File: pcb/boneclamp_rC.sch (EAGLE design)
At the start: 129 parts, among them IC1 24C, U1 AD8032ARZ-REEL7, U10 ADA4841-2YRZ, U11 ADA4841-2YRZ, U2 LT1964ES5-5TRMPBF, U3 ADA4841-2YRZ, U4 TLV70245DBVT, U5 ADA4841-2YRZ, U6 AD713JRZ-16, U7 AD7682BCPZ, U8 TPS63700DRCT, U9 ADA4841-2YRZ

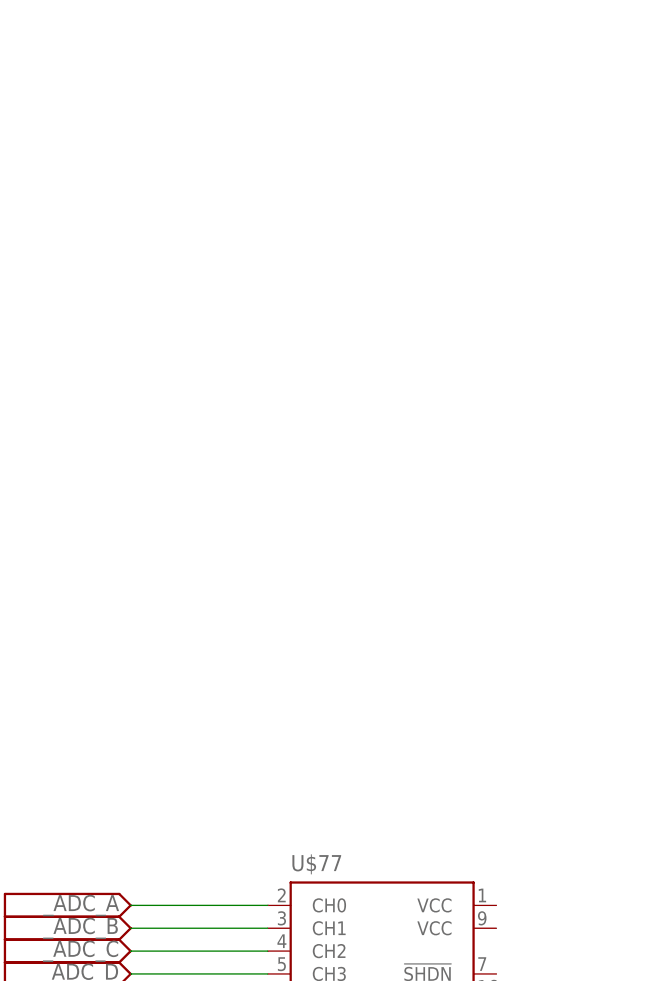
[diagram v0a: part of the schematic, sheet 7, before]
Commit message: Added the 8331 to schematic. I'm pretty sure this is the right ADC.
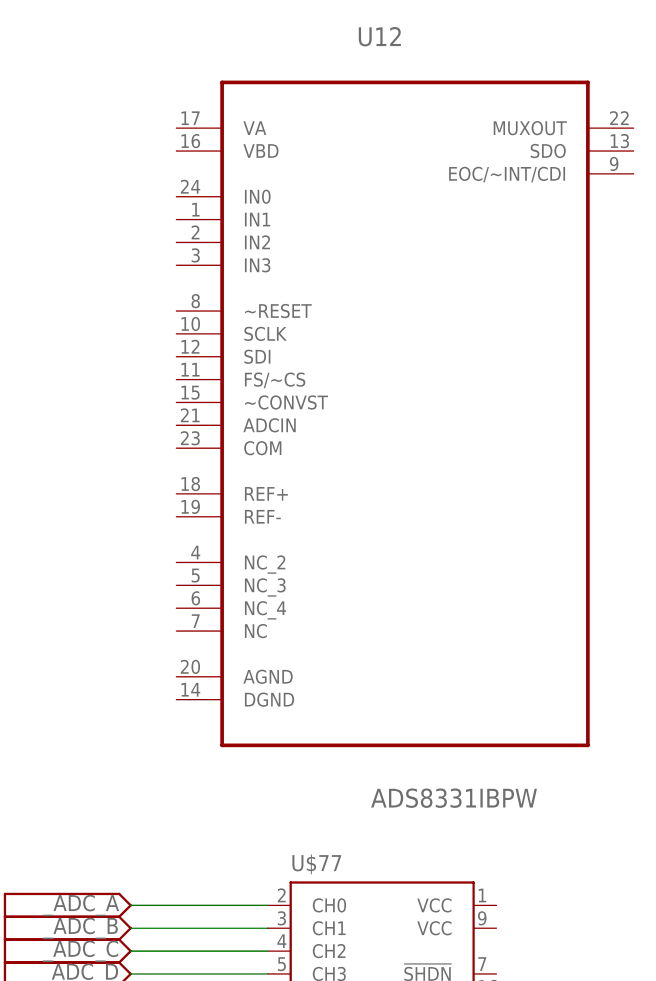
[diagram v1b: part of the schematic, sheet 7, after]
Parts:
- added U12: ADS8331IBPW, ti-extended:ADS8331IBPW
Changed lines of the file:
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@@
 <part name="U$76" library="boneclamp" deviceset="V_SIG" device=""/>
 <part name="U$82" library="boneclamp" deviceset="V_SIG" device=""/>
+<part name="U12" library="ti-extended" deviceset="ADS8331IBPW" device=""/>
 </parts>
 <sheets>
@@
 <instance part="U$80" gate="G$1" x="-27.94" y="7.62" rot="MR0"/>
 <instance part="U$81" gate="G$1" x="-27.94" y="5.08" rot="MR0"/>
+<instance part="U12" gate="A" x="2.54" y="71.12"/>
 </instances>
 <busses>

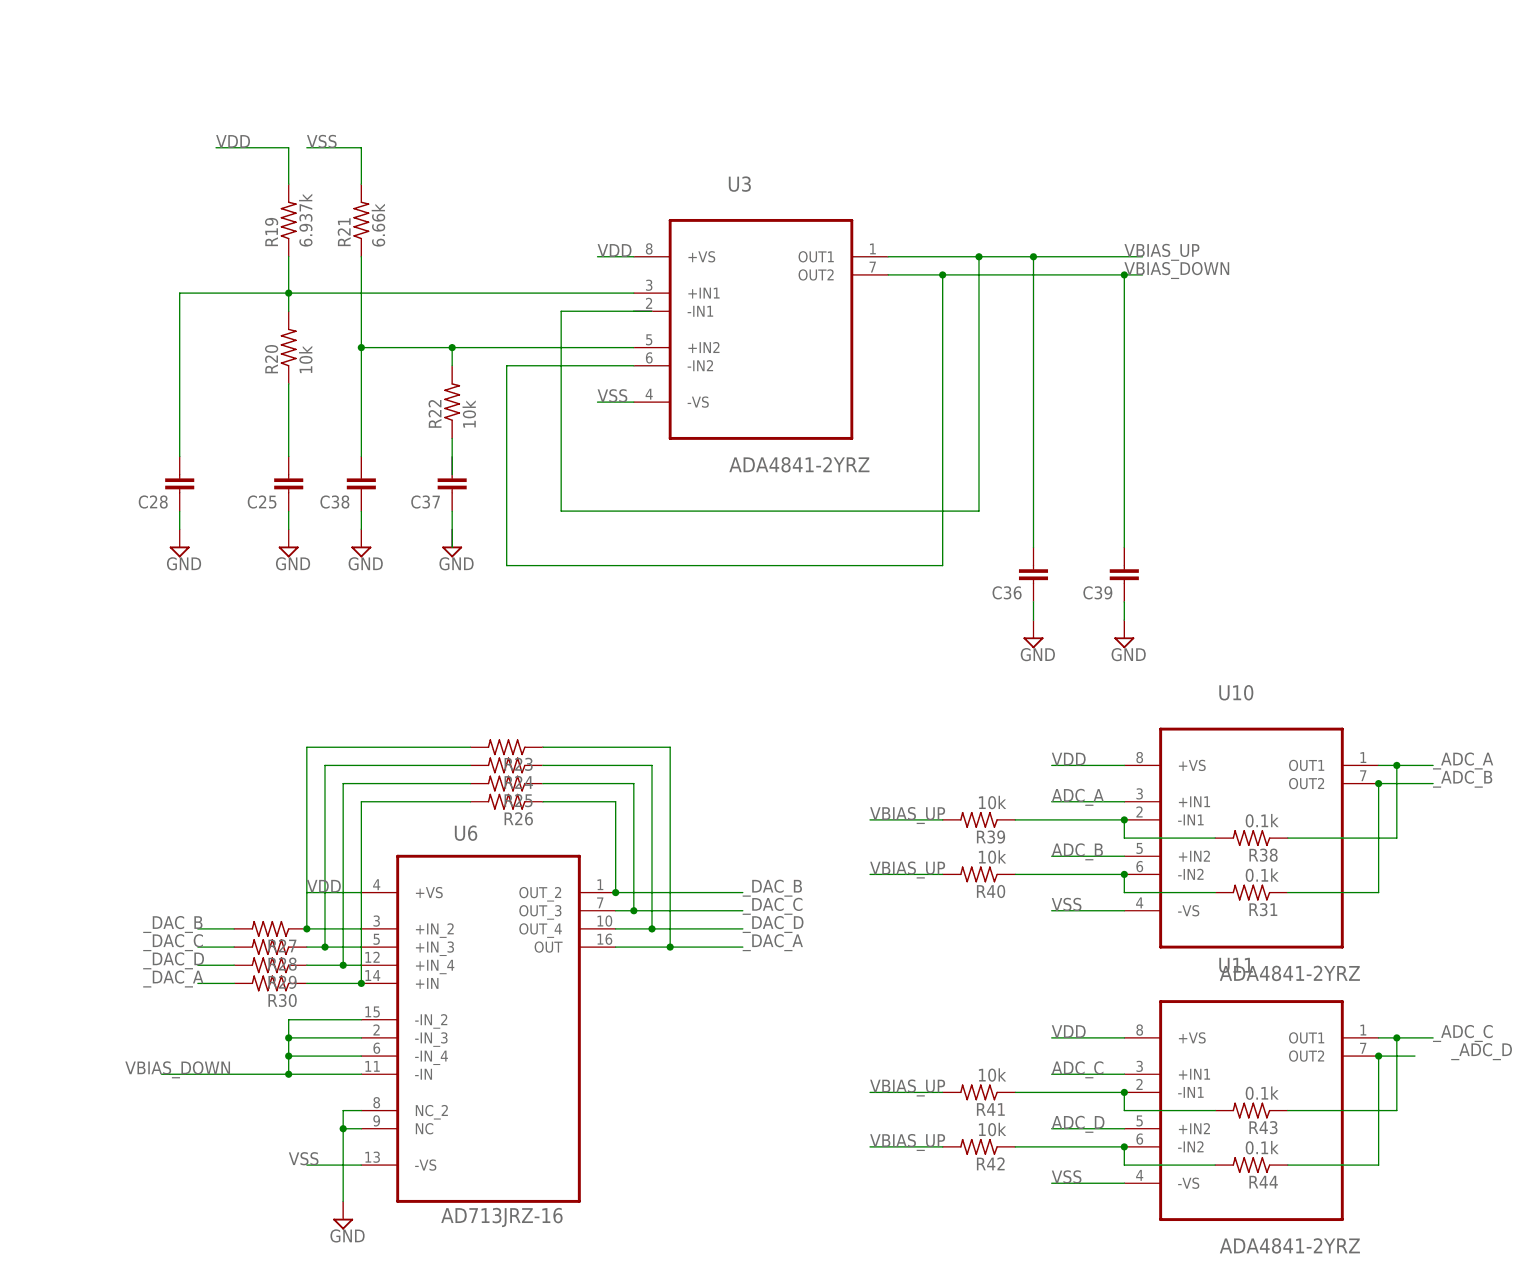
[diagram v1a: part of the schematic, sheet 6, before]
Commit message: Minor fixes to voltage bias followers
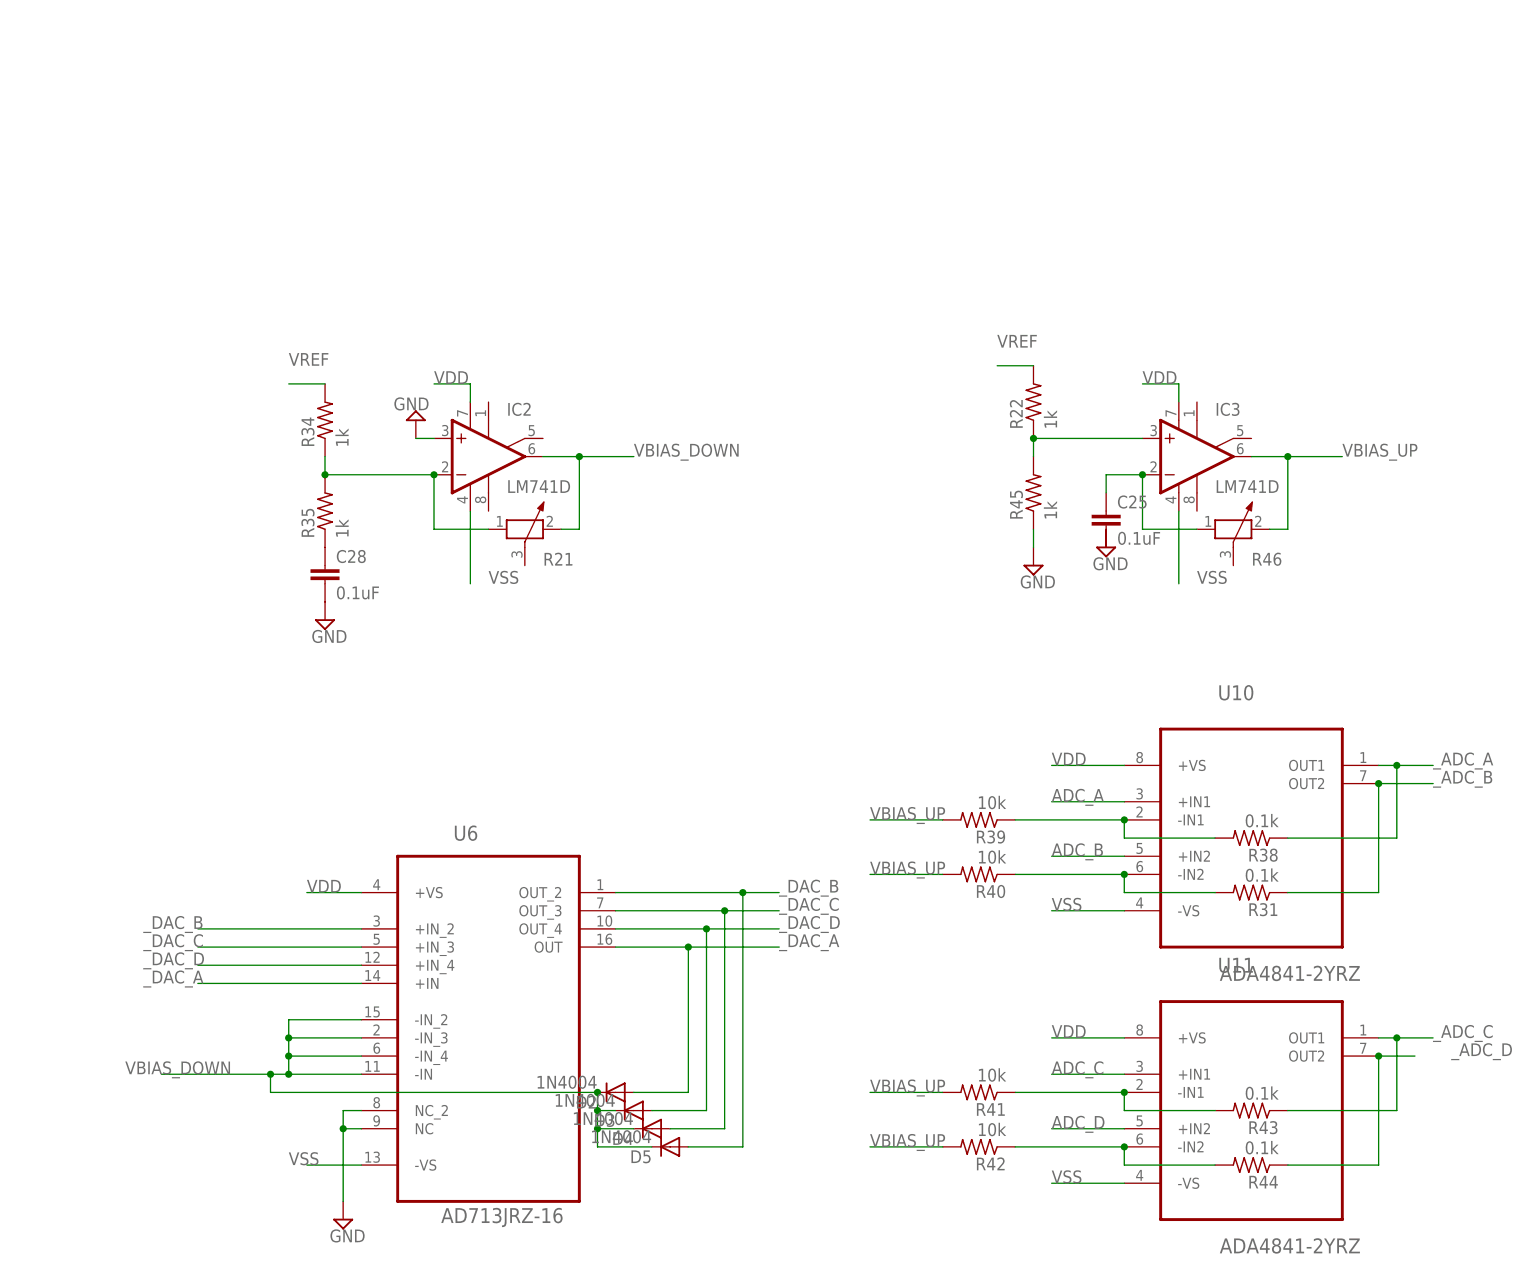
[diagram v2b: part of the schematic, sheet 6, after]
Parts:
- removed C36, C37, C38, C39: (no value), resistor:C-EU025-025X050
- removed R19: 6.937k, resistor:R-US_0204/2V
- removed R20: 10k, resistor:R-US_0204/2V
- removed R23, R24, R25, R26, R27, R28, R29, R30: (no value), resistor:R-US_0204/2V
- removed U3: ADA4841-2YRZ, analog-devices-01:ADA4841-2YRZ
- added D2, D3, D4, D5: 1N4004, diode:1N4004
- added IC2, IC3: LM741D, linear:LM741D
- added R34, R35, R45: 1k, resistor:R-US_0204/2V
- added R46: (no value), rcl:POTENTIOMETER_PT-10S
- C25, C28: value (none) -> 0.1uF; device resistor:C-EU025-025X050 -> rcl:C-EUC0805
- R21: value 6.66k -> (none); device resistor:R-US_0204/2V -> rcl:POTENTIOMETER_PT-10S
- R22: value 10k -> 1k
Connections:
- removed net N$3: R26.2, R30.1, U6.+IN
- removed net N$52: R25.2, R29.1, U6.+IN_4
- removed net N$53: C38.2, R21.1, R22.2, U3.+IN2
- removed net N$54: C28.2, R19.1, R20.2, U3.+IN1
- removed net N$55: R24.2, R28.1, U6.+IN_3
- removed net N$56: R23.2, R27.1, U6.+IN_2
- removed net N$57: C25.2, R20.1
- removed net N$58: C37.1
- removed net N$59: R22.1
- new net .5VREF-: IC2.-IN, R21.1, R34.1, R35.2
- new net .5VREF-1: C25.1, IC3.-IN, R46.1
- new net N$10: IC3.+IN, R22.1, R45.2
- new net N$12: C28.1, R35.1
- net GND: now also C28.2, IC2.+IN, R45.1; no longer C25.1, C28.1, C36.1, C38.1, C39.1
- net VBIAS_DOWN: now also D2.C, D3.C, D4.C, D5.C, IC2.OUT, R21.2; no longer C39.2, U3.-IN2, U3.OUT2
- net VBIAS_UP: now also IC3.OUT, R46.2; no longer C36.2, U3.-IN1, U3.OUT1
- net VDD: now also IC2.V+, IC3.V+; no longer R19.2, U3.+VS
- net VREF: now also R22.2, R34.2
- net VSS: now also IC2.V-, IC3.V-; no longer R21.2, U3.-VS
- net _DAC_A: now also D2.A, U6.+IN; no longer R23.1, R30.2
- net _DAC_B: now also D5.A, U6.+IN_2; no longer R26.1, R27.2
- net _DAC_C: now also D4.A, U6.+IN_3; no longer R25.1, R28.2
- net _DAC_D: now also D3.A, U6.+IN_4; no longer R24.1, R29.2
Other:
- moved on the sheet: C25, C28, R22

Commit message: Finished basics of input stage to new 8331 and some of the digital interface for it.
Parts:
- removed C11: 10uF, rcl:C-EUC0805
- removed C12, C13, C14: 0.1uF, rcl:C-EUC0805
- removed SJ6, SJ7, SJ8: (no value), jumper:SJ
- removed U$77: ADS8343, ti-extended:ADS8343
- removed U7: AD7682BCPZ, analog-devices-02:AD7682BCPZ
- added C36, C37: 0.1uF, rcl:C-EUC0603
- added C39, C47: 1uF, rcl:C-EUC0603
- added C48: (no value), rcl:C-EUC0805
- added C55, C56: 4.7uF, rcl:C-EUC0603
- added C57, C58, C59, C64, C65, C66, C67, C68, C69: 0.1uF, rcl:C-EUC0805
- added C60, C61, C62, C63: 1nF, rcl:C-EUC0603
- added R19, R20, R29, R30, R47, R48, R49, R50: 10k, rcl:R-US_R0603
- added R23: 10k,1%, resistor:R-US_R0805
- added R24: 1k, resistor:R-US_R0805
- added R25, R26, R27, R28: 20, rcl:R-US_R0603
- added R51: 20k,1%, resistor:R-US_R0805
- added SJ5, SJ9: (no value), jumper:SJ
- added TP8, TP9: TPB1,27, testpad:TPB1,27
- added U13, U15, U16, U3: OPA365AIDBVR, ti-extended:OPA365AIDBVR
- added U14: REF5040MDREP, ti-extended:REF5040MDREP
- U$63: value ADS8343 -> OPA735BVT; device ti-extended:ADS8343 -> ti-extended:OPA735BVT
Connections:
- removed net ADC_SCLK: U7.SCK
- removed net ADC_SDI: SJ7.1
- removed net ADC_SDID: SJ8.1
- removed net N$11: SJ7.2, SJ8.2, U7.DIN
- removed net N$28: C11.1, R14.2, U7.REF
- removed net N$34: C14.1, U7.REFIN
- removed net VCOM: U7.COM
- new net ADC_CDI: SJ9.1
- new net ADC_CS: U12.FS/~CS
- new net AGND1: C57.2, U12.DGND
- new net N$13: R47.1, R48.2, U15.-IN
- new net N$15: R49.1, R50.2, U16.-IN
- new net N$24: U12.ADCIN, U12.MUXOUT
- new net N$26: R23.1, R51.2, U$63.-IN
- new net N$3: R19.1, R20.2, U3.-IN
- new net N$32: C47.2, U14.TRIM/NR
- new net N$35: SJ5.2, U12.SDO
- new net N$36: SJ9.2, U12.EOC/~INT/CDI
- new net N$37: C55.1, C56.1, C60.1, C61.1, C62.1, C63.1, U12.AGND, U12.REF-
- new net N$40: C60.2, R25.1, U12.IN0
- new net N$41: C61.2, R26.1, U12.IN1
- new net N$42: C62.2, R27.1, U12.IN2
- new net N$43: C63.2, R28.1, U12.IN3
- new net N$6: R29.1, R30.2, U13.-IN
- new net VBIAS+: U13.+IN, U15.+IN, U16.+IN, U3.+IN
- new net VBIAS-: C3.1, R23.2, R24.1, TP8.TP
- new net _VREF: C48.1, R14.2, R51.1, TP9.TP, U14.VOUT
- net ADC_A: now also R19.2
- net ADC_B: now also R29.2
- net ADC_C: now also R47.2
- net ADC_CNV: now also U12.~CONVST; no longer U7.CNV
- net ADC_D: now also R49.2
- net ADC_SDO: now also SJ5.1; no longer SJ6.2
- net AGND: now also C36.1, C37.1, C39.1, C47.1, C48.2, C58.2, C59.2, C64.2, C65.2, C66.2, C67.2, C68.2, C69.2, U$63.+IN, U14.GND; no longer C11.2, C12.2, C13.2, C14.2, U$42.GAIN, U7.EP, U7.GND, U7.GND_2
- net N$9: now also R24.2, U$63.VOUT-; no longer SJ6.1
- net VDD: now also C37.2, C39.2, C55.2, C59.1, C65.1, C67.1, C69.1, U$63.V+, U12.VA, U13.V+, U14.VIN, U15.V+, U16.V+, U3.V+; no longer C13.1, C3.1, U7.VDD, U7.VDD_2
- net VDRIVE: now also C57.1, U$42.GAIN, U12.VBD; no longer C12.1, U7.VIO
- net VREF: now also C56.2, U12.REF+
- net VSS: now also C36.2, C58.1, C64.1, C66.1, C68.1, U$63.V-, U13.V-, U15.V-, U16.V-, U3.V-
- net _ADC_A: now also R20.1, R25.2, U3.VOUT; no longer U7.IN0
- net _ADC_B: now also R26.2, R30.1, U13.VOUT; no longer U7.IN1
- net _ADC_C: now also R27.2, R48.1, U15.VOUT; no longer U7.IN2
- net _ADC_D: now also R28.2, R50.1, U16.VOUT; no longer U7.IN3
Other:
- note added: "Connect REF- to AGND using single, isolated via."
- note added: "I have not figured out how daisy chain will work."
- note added: "Output capacitor: C >= 1.0uF 1.0<= ESR <= 1.5 Ohms."
